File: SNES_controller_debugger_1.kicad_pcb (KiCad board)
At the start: 2 copper layers, 100 x 74 mm, 22 parts, among them J1 ICSP, J2 CONTROLLER_OUT, J3 MICRO_USB, SW1 Reset, U1 ATmega32U4, Y1 16MHz

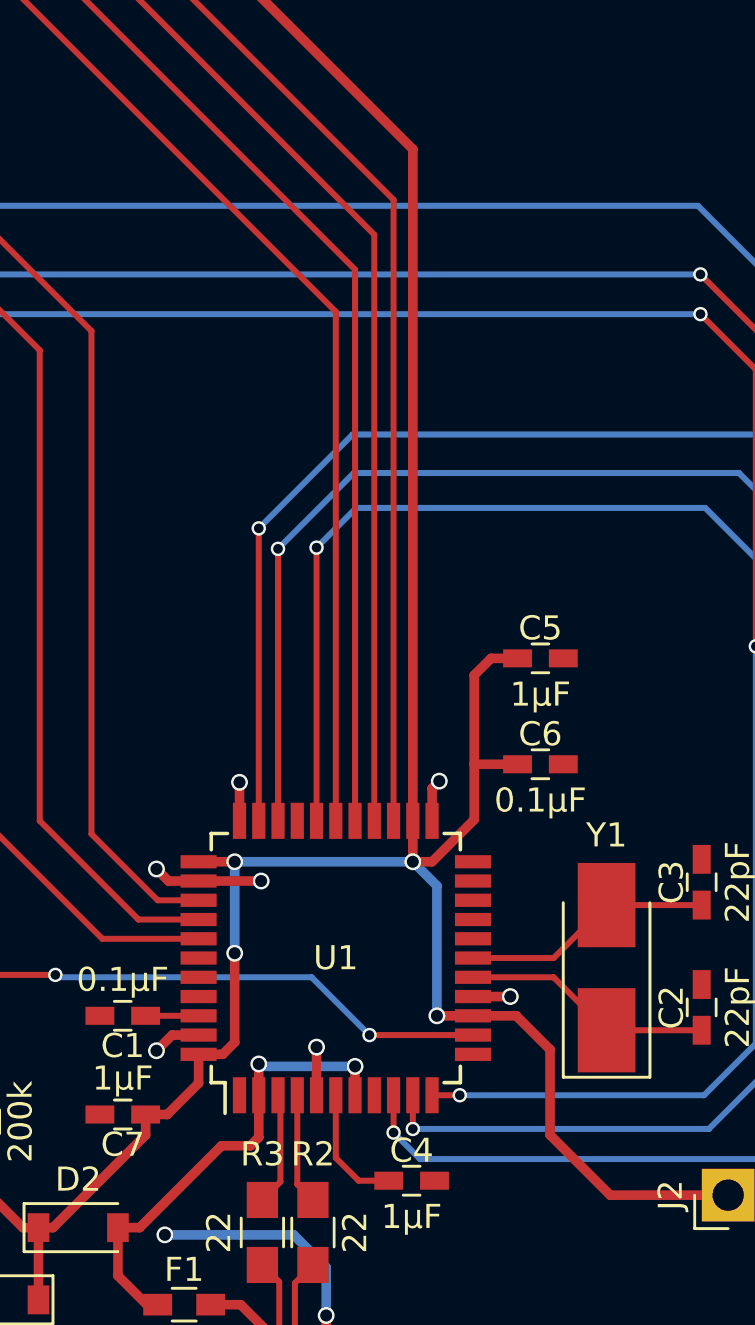
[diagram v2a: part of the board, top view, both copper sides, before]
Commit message: pcb: Move C5 and C6 nearer to the MCU.
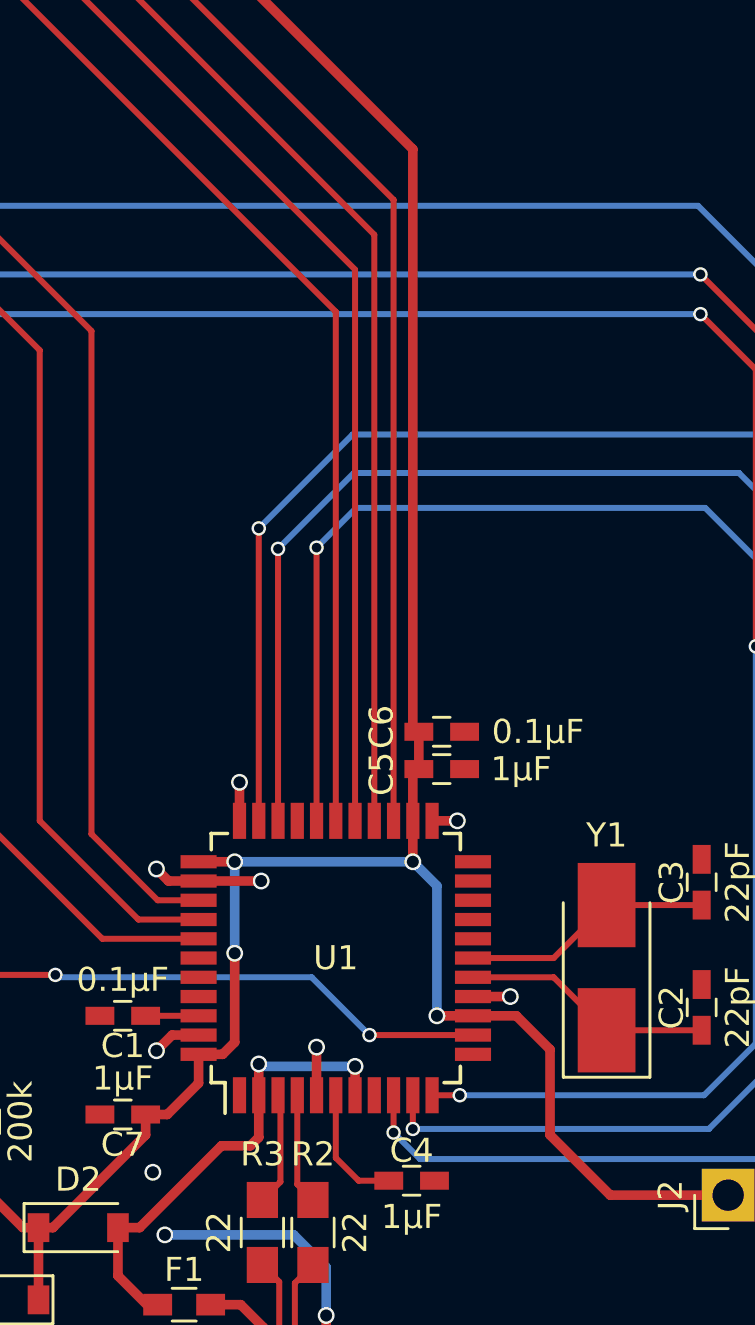
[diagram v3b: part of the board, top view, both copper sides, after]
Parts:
- moved C5 6.16 mm to (136.1, 132.3)
- moved C6 4.32 mm to (136.1, 130.8)
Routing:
- net VCC: track 234.9 -> 221.9 mm
- net Earth: track 24.6 -> 23.9 mm
- net (no net): vias 0 -> 1
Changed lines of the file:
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@@
     (thickness 1.6)
     (drawings 5)
-    (tracks 238)
+    (tracks 235)
     (zones 0)
     (modules 22)
@@
   (layers
     (0 F.Cu signal)
-    (31 B.Cu signal hide)
+    (31 B.Cu signal)
     (32 B.Adhes user hide)
     (33 F.Adhes user hide)
@@
   )
   (module Capacitors_SMD:C_0603_HandSoldering (layer F.Cu)
-    (at 140.2 127.7)
+    (at 136.1 132.3)
     (descr "Capacitor SMD 0603, hand soldering")
     (tags "capacitor 0603")
     (attr smd)
-    (fp_text reference C5 (at 0 -1.25) (layer F.SilkS)
-      (effects (font (size 1 1) (thickness 0.15)))
-    )
-    (fp_text value 1µF (at 0 1.5) (layer F.SilkS)
+    (fp_text reference C5 (at -2.5 0.2 90) (layer F.SilkS)
+      (effects (font (size 1 1) (thickness 0.15)))
+    )
+    (fp_text value 1µF (at 3.3 0) (layer F.SilkS)
       (effects (font (size 1 1) (thickness 0.15)))
     )
@@
   )
   (module Capacitors_SMD:C_0603_HandSoldering (layer F.Cu)
-    (at 140.2 132.1)
+    (at 136.1 130.75)
     (descr "Capacitor SMD 0603, hand soldering")
     (tags "capacitor 0603")
     (attr smd)
-    (fp_text reference C6 (at 0 -1.25) (layer F.SilkS)
-      (effects (font (size 1 1) (thickness 0.15)))
-    )
-    (fp_text value 0.1µF (at 0 1.5) (layer F.SilkS)
+    (fp_text reference C6 (at -2.5 -0.2 90) (layer F.SilkS)
+      (effects (font (size 1 1) (thickness 0.15)))
+    )
+    (fp_text value 0.1µF (at 4 0) (layer F.SilkS)
       (effects (font (size 1 1) (thickness 0.15)))
     )
@@
   (gr_line (start 179 161) (end 79 161) (angle 90) (layer Edge.Cuts) (width 0.15))
   (gr_line (start 179 87) (end 179 161) (angle 90) (layer Edge.Cuts) (width 0.15))
+  (via (at 124.1 149.05) (size 0.7) (drill 0.5) (layers F.Cu B.Cu) (net 0))
   (segment (start 126 142.55) (end 123.8 142.55) (width 0.25) (layer F.Cu) (net 1))
+  (segment (start 135.7 134.45) (end 136.75 134.45) (width 0.4) (layer F.Cu) (net 2))
+  (via (at 136.75 134.45) (size 0.7) (drill 0.5) (layers F.Cu B.Cu) (net 2))
   (segment (start 126 143.35) (end 124.9 143.35) (width 0.4) (layer F.Cu) (net 2))
   (via (at 124.25 144) (size 0.7) (drill 0.5) (layers F.Cu B.Cu) (net 2))
@@
   (segment (start 137.4 141.75) (end 138.95 141.75) (width 0.4) (layer F.Cu) (net 2))
   (via (at 138.95 141.75) (size 0.7) (drill 0.5) (layers F.Cu B.Cu) (net 2))
-  (segment (start 135.7 134.45) (end 135.7 133.1) (width 0.4) (layer F.Cu) (net 2))
-  (via (at 136 132.8) (size 0.7) (drill 0.5) (layers F.Cu B.Cu) (net 2))
-  (segment (start 135.7 133.1) (end 136 132.8) (width 0.4) (layer F.Cu) (net 2))
   (segment (start 126 136.95) (end 128.6 136.95) (width 0.4) (layer F.Cu) (net 2))
   (via (at 128.6 136.95) (size 0.7) (drill 0.5) (layers F.Cu B.Cu) (net 2))
@@
   (segment (start 129.4 149.45) (end 129.4 145.95) (width 0.25) (layer F.Cu) (net 25))
   (segment (start 129.4 145.95) (end 129.3 145.85) (width 0.25) (layer F.Cu) (net 25))
+  (segment (start 134.9 130.5) (end 134.9 106.55) (width 0.4) (layer F.Cu) (net 26))
+  (segment (start 134.9 106.55) (end 125.56 97.21) (width 0.4) (layer F.Cu) (net 26))
+  (segment (start 125.56 97.21) (end 125.56 90) (width 0.4) (layer F.Cu) (net 26))
+  (segment (start 134.9 130.5) (end 135.15 130.75) (width 0.4) (layer F.Cu) (net 26))
+  (segment (start 135.15 132.3) (end 135.15 130.75) (width 0.4) (layer F.Cu) (net 26))
+  (segment (start 134.9 134.45) (end 134.9 132.55) (width 0.4) (layer F.Cu) (net 26))
+  (segment (start 134.9 132.55) (end 135.15 132.3) (width 0.4) (layer F.Cu) (net 26))
   (segment (start 137.4 142.55) (end 139.2 142.55) (width 0.4) (layer F.Cu) (net 26))
   (segment (start 143.1 150) (end 148 150) (width 0.4) (layer F.Cu) (net 26))
@@
   (segment (start 123.8 147.5) (end 123.8 146.65) (width 0.4) (layer F.Cu) (net 26))
   (segment (start 119.95 151.35) (end 123.8 147.5) (width 0.4) (layer F.Cu) (net 26))
-  (segment (start 139.25 132.1) (end 137.45 132.1) (width 0.4) (layer F.Cu) (net 26))
-  (segment (start 134.9 136.15) (end 135.7 136.15) (width 0.4) (layer F.Cu) (net 26))
-  (segment (start 135.7 136.15) (end 137.45 134.4) (width 0.4) (layer F.Cu) (net 26))
-  (segment (start 137.45 134.4) (end 137.45 132.1) (width 0.4) (layer F.Cu) (net 26))
-  (segment (start 138.15 127.7) (end 139.25 127.7) (width 0.4) (layer F.Cu) (net 26))
-  (segment (start 137.45 128.4) (end 138.15 127.7) (width 0.4) (layer F.Cu) (net 26))
-  (segment (start 137.45 132.1) (end 137.45 128.4) (width 0.4) (layer F.Cu) (net 26))
-  (segment (start 134.9 134.45) (end 134.9 106.55) (width 0.4) (layer F.Cu) (net 26))
-  (segment (start 125.56 97.21) (end 125.56 90) (width 0.4) (layer F.Cu) (net 26))
-  (segment (start 134.9 106.55) (end 125.56 97.21) (width 0.4) (layer F.Cu) (net 26))
   (segment (start 134.9 136.15) (end 135.9 137.15) (width 0.4) (layer B.Cu) (net 26))
   (via (at 135.9 142.55) (size 0.7) (drill 0.5) (layers F.Cu B.Cu) (net 26))

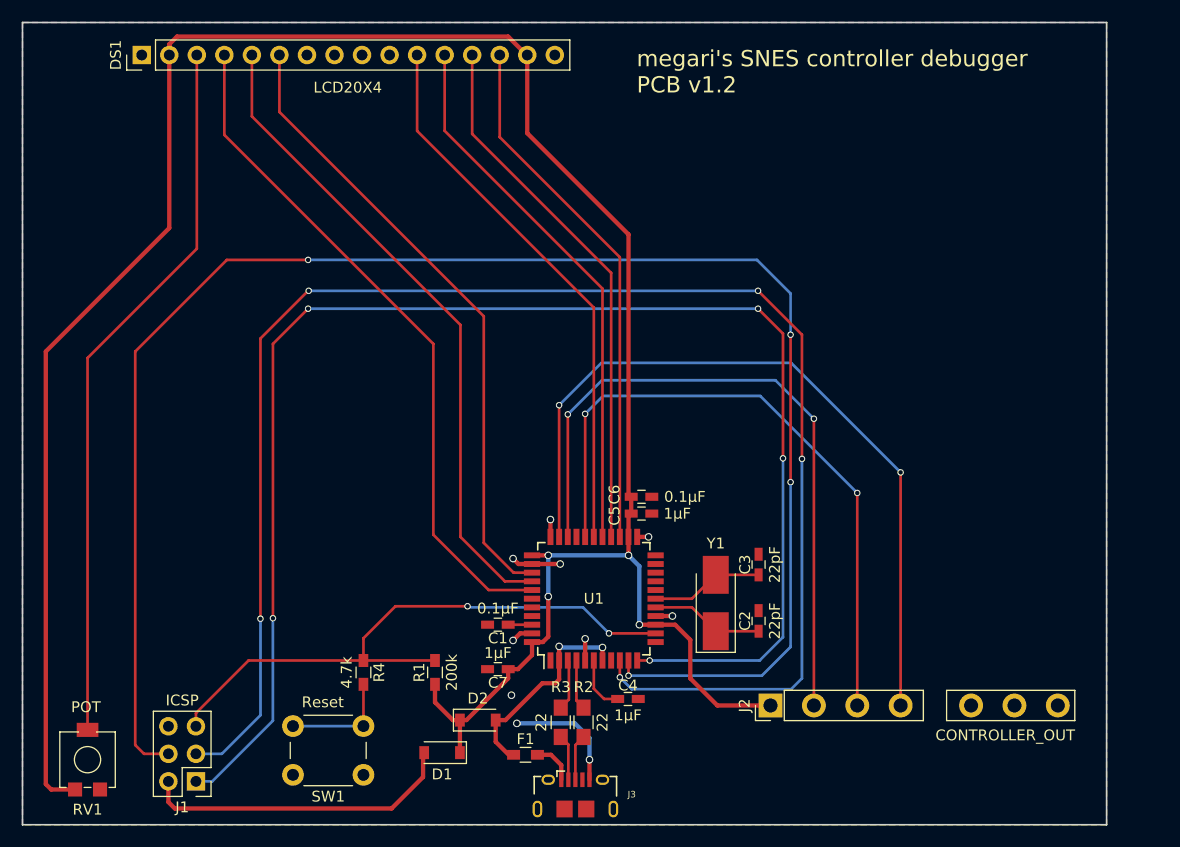
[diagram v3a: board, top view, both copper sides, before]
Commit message: pcb: Another complete overhaul under the supervision of Icchan^.
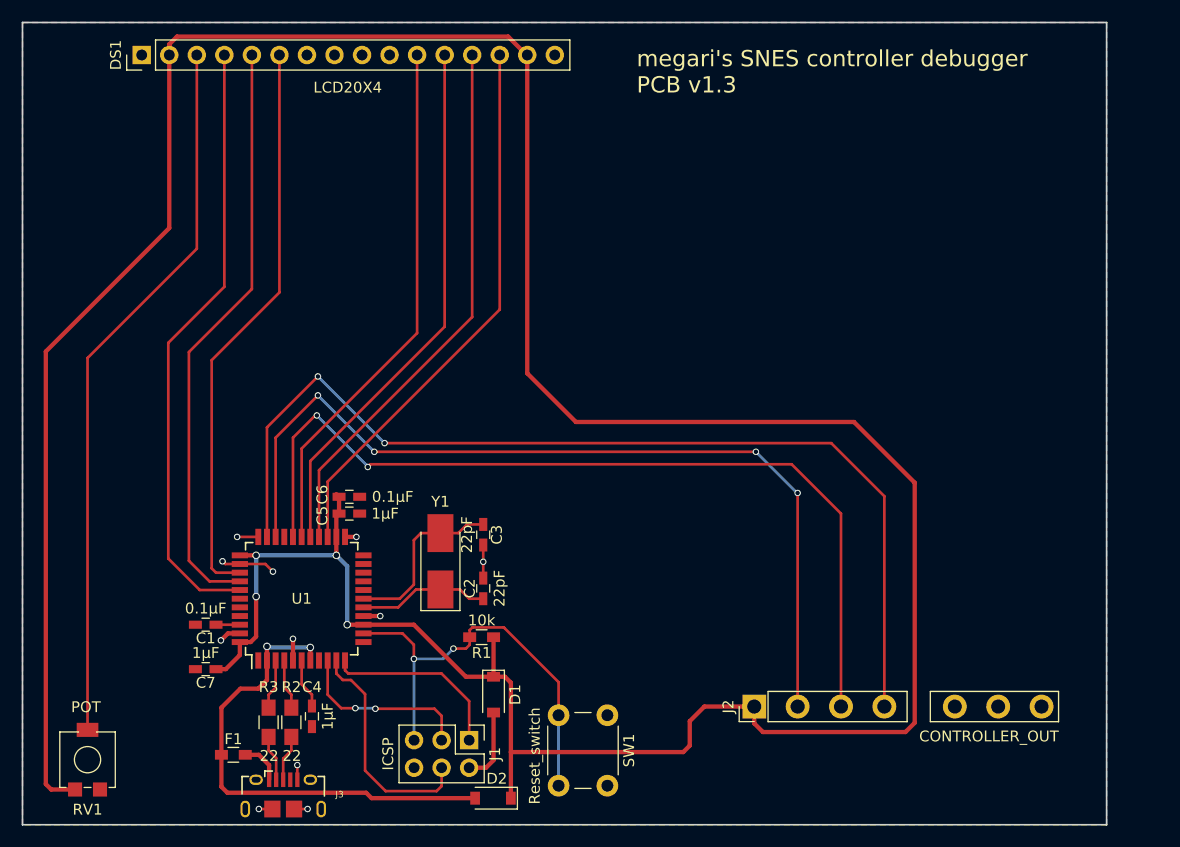
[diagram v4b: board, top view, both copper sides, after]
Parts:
- removed R4: 4.7k, Resistors_SMD:R_0603_HandSoldering
- D1, D2: value MBR0520 -> (none)
- R1: value 200k -> 10k
- SW1: value Reset -> Reset_switch
- moved C4 29.2 mm to (105.7, 151.0), turned to 270 degrees
- moved F1 27.0 mm to (98.5, 154.6)
- moved J3 27.0 mm to (103.0, 159.6)
- moved R2 27.0 mm to (103.8, 151.6)
- moved R3 27.0 mm to (101.7, 151.6)
- moved C1 26.9 mm to (95.9, 142.6)
- moved C5 26.9 mm to (109.2, 132.3)
- moved C6 26.9 mm to (109.2, 130.8)
- moved C7 26.9 mm to (95.9, 146.7)
- moved U1 26.9 mm to (104.8, 140.2)
- moved Y1 25.7 mm to (117.5, 136.7)
- moved C2 25.6 mm to (121.5, 139.2)
- moved C3 25.5 mm to (121.5, 134.2), turned to 270 degrees
- moved J1 25.5 mm to (120.2, 153.2), turned to 270 degrees
- moved SW1 23.2 mm to (132.9, 150.9), turned to 270 degrees
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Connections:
- DS1 pad 10: (no net) -> Net-(DS1-Pad10)
- DS1 pad 7: (no net) -> Net-(DS1-Pad7)
- DS1 pad 8: (no net) -> Net-(DS1-Pad8)
- DS1 pad 9: (no net) -> Net-(DS1-Pad9)
- J2 pad 5: (no net) -> Net-(J2-Pad5)
- J2 pad 6: (no net) -> Net-(J2-Pad6)
- J3 pad 4: (no net) -> Net-(J3-Pad4)
- SW1 pad 2: Net-(R4-Pad2) -> RESET
- U1 pad 1: (no net) -> Net-(U1-Pad1)
- U1 pad 12: (no net) -> Net-(U1-Pad12)
- U1 pad 18: (no net) -> Net-(U1-Pad18)
- U1 pad 19: (no net) -> Net-(U1-Pad19)
- U1 pad 20: (no net) -> Net-(U1-Pad20)
- U1 pad 21: (no net) -> Net-(U1-Pad21)
- U1 pad 22: (no net) -> Net-(U1-Pad22)
- U1 pad 30: (no net) -> Net-(U1-Pad30)
- U1 pad 39: (no net) -> Net-(U1-Pad39)
- U1 pad 40: (no net) -> Net-(U1-Pad40)
- U1 pad 41: (no net) -> Net-(U1-Pad41)
- U1 pad 8: (no net) -> Net-(U1-Pad8)
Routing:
- net MOSI: track 155.0 -> 21.4 mm, vias 4 -> 0
- net SCLK: track 146.5 -> 16.7 mm, vias 5 -> 2
- net MISO: track 135.9 -> 17.1 mm, vias 5 -> 0
- net VCC: track 221.9 -> 311.2 mm
- net UVCC: track 19.8 -> 45.2 mm
- net IVCC: track 29.2 -> 6.94 mm
- net DATA_IN: track 70.9 -> 93.0 mm
- net LATCH_OUT: track 60.4 -> 82.3 mm
- net CLK_OUT: track 63.2 -> 82.3 mm, vias 2 -> 4
- net RESET: track 56.5 -> 40.9 mm
- net Net-(R4-Pad2): track 10.4 -> 0.00 mm
- net LCD_RS: track 63.4 -> 56.4 mm
- net LCD_RW: track 60.7 -> 54.5 mm
- net Net-(C3-Pad1): track 10.4 -> 16.3 mm
- net LCD_E: track 58.4 -> 52.7 mm
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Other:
- net class GND added: clearance 0.2, trace_width 0.25, via_dia 0.6, via_drill 0.4
- net class USB added: clearance 0.2, trace_width 0.25, via_dia 0.6, via_drill 0.4
- board text added: "megari's SNES controller debugger PCB v1.3"
- board text removed: "megari's SNES controller debugger PCB v1.2"

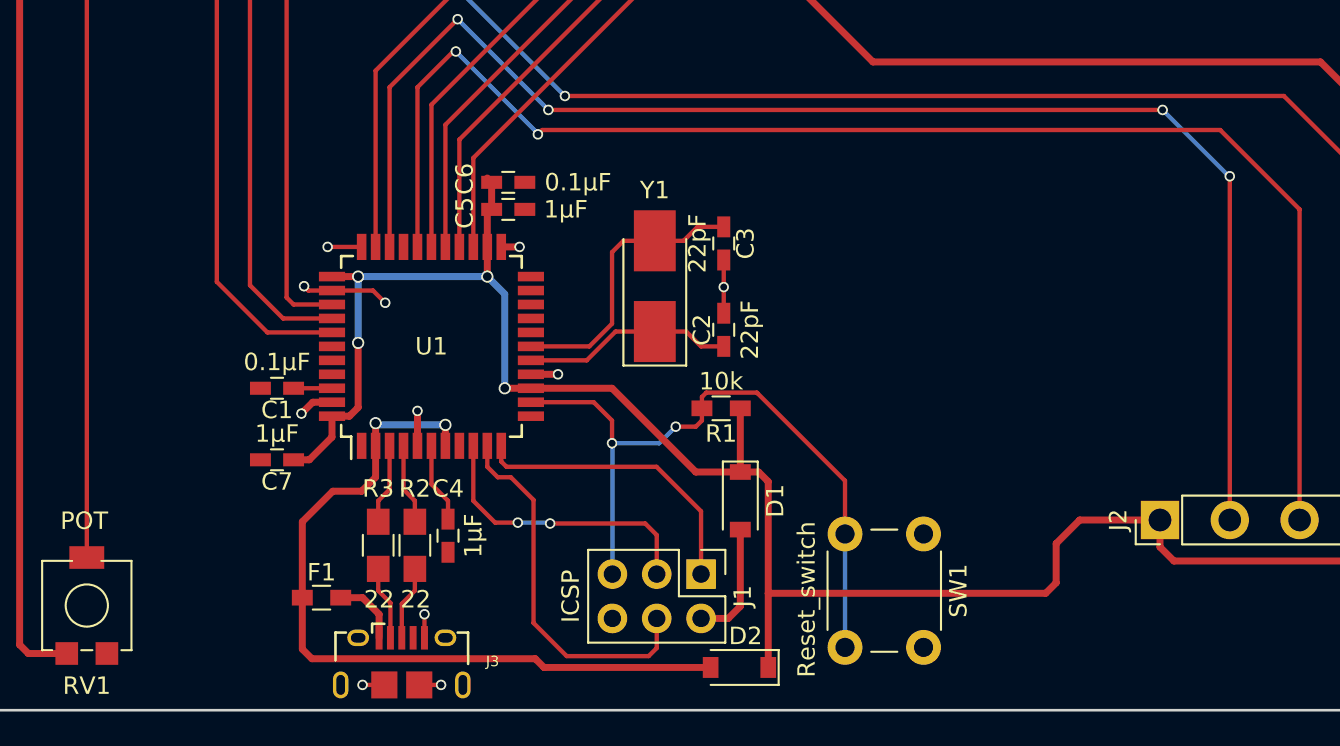
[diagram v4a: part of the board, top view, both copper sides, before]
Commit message: pcb: Work on reducing the number and length of traces on the back side to make the ground plane more unified.
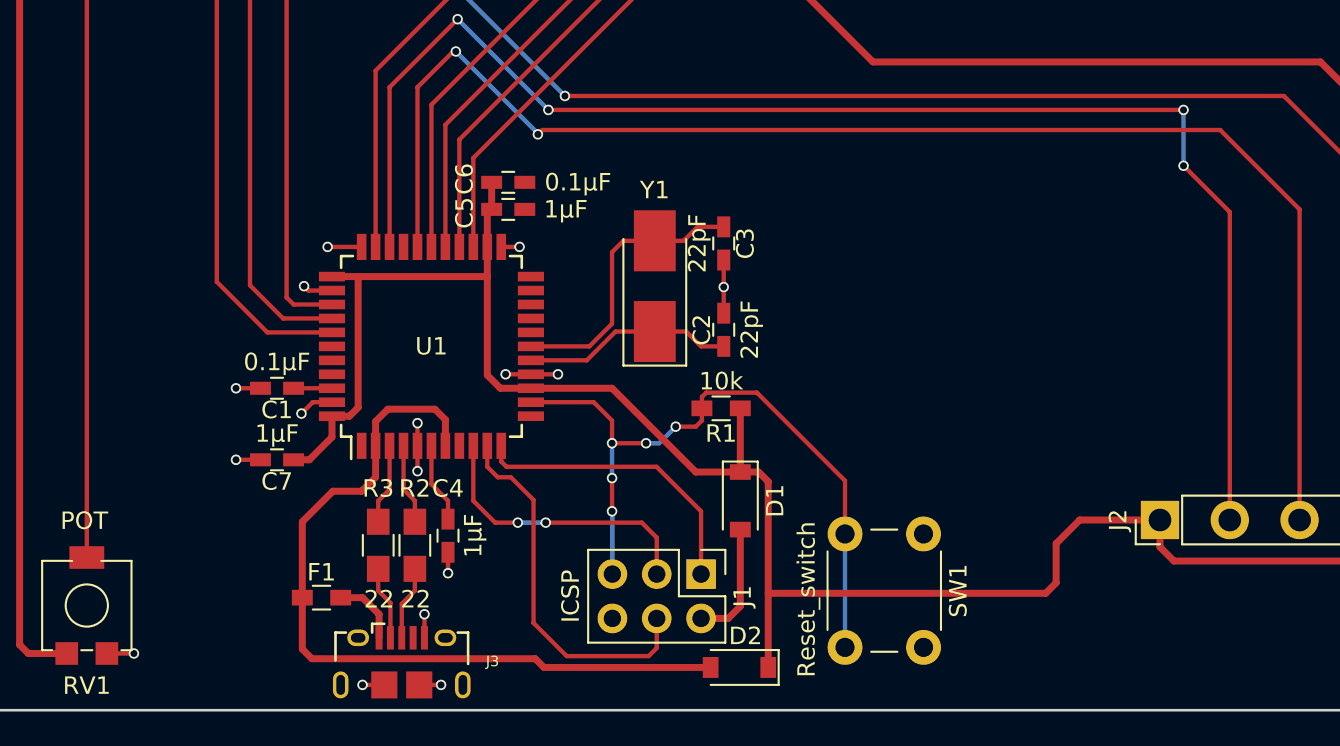
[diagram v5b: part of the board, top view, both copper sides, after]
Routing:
- net Earth: track 20.5 -> 24.9 mm, vias 11 -> 16
- net UVCC: track 45.2 -> 46.1 mm, vias 2 -> 0
- net CLK_OUT: track 82.3 -> 83.0 mm
- net VCC: track 311.2 -> 311.0 mm, vias 4 -> 0
- net RESET: vias 2 -> 5
